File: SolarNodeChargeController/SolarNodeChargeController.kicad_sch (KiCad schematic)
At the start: 36 parts, among them J1 Solar_5V, J2 Solar_5V, J3 Solar_5V, J4 Solar_5V, J5 LiPo_1S_4.2V, J6 VOUT, J7 SW_BATT, J8 SW_LOAD, J9 I2C_MCU, Q1 AO3401A, SW3 SOLAR / BATT, U1 CN3791, U2 INA219AID

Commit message: feat: shrink board to 42x26 mm with SMD diodes and 1.25 mm connectors
Input diodes: D5-D8 move from DO-41 1N5819 to SOD-323 1N5819WS (same
40V/1A rating and pinout). The panels peak at ~200-300 mA each, so the
large through-hole part bought nothing and cost ~12 mm of board width.

Connectors: every power connector (solar J1-J4, battery J5, VOUT J6,
switch leads J7/J8) becomes a 2-pin Micro JST 1.25 / Molex PicoBlade
vertical header (53047-0210), and the I2C header J9 a 4-pin one
(53047-0410). The trade-off is that power connectors are no longer
keyed against each other, so the docs call for clear silkscreen labels.

Charge current: R5 0.12R -> 0.15R lowers it from 1.0 A to 0.8 A, leaving
margin on the 1.0 A-rated PicoBlade contacts on the battery path.

The placement draft is rebuilt around the smaller parts: 60x29 -> 42x26
mm, 0 courtyard overlaps, 0 schematic-parity issues, ERC clean.

gen-schematic.js now derives UUIDs from each item's identity (symbol
ref, wire endpoints, label name and position) instead of random ones.
Regenerating an unchanged design is byte-identical, and symbol UUIDs,
which the PCB footprints link to, no longer churn on every run.

README, CLAUDE.md and the README images are updated to match. The
.kicad_pro change is KiCad writing its default settings when the
project was opened.

Co-Authored-By: Claude Opus 5.5 <noreply@anthropic.com>
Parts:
- removed D5, D6, D7, D8: 1N5819, Diode_THT:D_DO-41_SOD81_P10.16mm_Horizontal, symbol Diode:1N5819
- added D5, D6, D7, D8: 1N5819WS, Diode_SMD:D_SOD-323, symbol Diode:1N5819WS
- J1, J2, J3, J4, J5, J6: footprint Connector_JST:JST_PH_B2B-PH-K_1x02_P2.00mm_Vertical -> Connector_Molex:Molex_PicoBlade_53047-0210_1x02_P1.25mm_Vertical
- J7, J8: footprint Connector_JST:JST_XH_B2B-XH-A_1x02_P2.50mm_Vertical -> Connector_Molex:Molex_PicoBlade_53047-0210_1x02_P1.25mm_Vertical
- J9: footprint Connector_PinHeader_2.54mm:PinHeader_1x04_P2.54mm_Vertical -> Connector_Molex:Molex_PicoBlade_53047-0410_1x04_P1.25mm_Vertical
- R5: value 0.12R 1% -> 0.15R 1%
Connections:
- net PV: now also D5.1 (K), D6.1 (K), D7.1 (K), D8.1 (K)
- net at J3.1 (Pin_1): now also D7.2 (A)
- net at J1.1 (Pin_1): now also D5.2 (A)
- net at J4.1 (Pin_1): now also D8.2 (A)
- net at J2.1 (Pin_1): now also D6.2 (A)
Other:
- note added: "Design notes (CN3791 datasheet, Figure 1): - Solar inputs J1-J4: up to four 5V panels in parallel, each isolated by a 1N5819WS (SOD-323, 40V/1A). MPPT senses VIN after these diodes, so each panel sits ~0.3-0.45V above the 4.6V setpoint (~4.9-5.0V, typical Vmp of a 5V panel). Panels peak at ~200-300mA each. - Charge current: ICH = 120mV / R5 = 120mV / 0.15R = 0.8A, leaving margin on the 1.0A conne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"
- note removed: "Design notes (CN3791 datasheet, Figure 1): - Solar inputs J1-J4: up to four 5V panels in parallel, each isolated by a 1N5819 (40V/1A). MPPT senses VIN after these diodes, so each panel sits ~0.3-0.45V above the 4.6V setpoint (~4.9-5.0V, typical Vmp of a 5V panel). One panel alone carries ~0.9A at 1A charge. - Charge current: ICH = 120mV / R5 = 120mV / 0.12R = 1.0A (R5 = 0.24R for 0.5A). - MPPT se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"
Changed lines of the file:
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@@
 		)
 	)
-	(text "Design notes (CN3791 datasheet, Figure 1):\n- Solar inputs J1-J4: up to four 5V panels in parallel, each isolated by a 1N5819 (40V/1A). MPPT senses VIN after these diodes,\n  so each panel sits ~0.3-0.45V above the 4.6V setpoint (~4.9-5.0V, typical Vmp of a 5V panel). One panel alone carries ~0.9A at 1A charge.\n- Charge current: ICH = 120mV / R5 = 120mV / 0.12R = 1.0A (R5 = 0.24R for 0.5A).\n- MPPT setpoint: VMPPT = 1.205V x (1 + R3/R4) = 1.205 x (1 + 28.0k/10k) = 4.58V. Charging starts once MPPT > 1.23V (VIN > 4.68V).\n- L1: datasheet requires L > 5 x (VCC - VBAT) uH = 16uH at 6V Voc / 2.8V batt. 22uH gives ~0.2A ripple at 6V in, 3.7V batt.\n- Datasheet blocking diode D1 omitted to save ~0.4V headroom: D5-D8 keep the battery out of the panels; the CN3791 then draws ~21uA\n  from the battery via L1 and Q1's body diode when dark (datasheet p.9). Reference D1 is intentionally unused.\n- Status: D4 red ON = charging, D3 green ON = charge done. Both off = no input or VIN < VBAT.\n- Panel-mount SPST switches plug into J7/J8 (JST-XH, 3A; PH is used for panels/battery so leads can't be swapped).\n  J7 SW_BATT isolates the cell from charger and load. J8 SW_LOAD switches only VOUT (J6), so the cell keeps charging with it off.\n  Rate both switches >= 1A or the module's peak current, whichever is higher (battery current is charge OR load, not the sum).\n  With SW_BATT off in sun the CN3791 sees no battery and VBAT pulses near 4.2V: keep SW_LOAD off then.\n- INA219 (U2, I2C 0x40 with A0=A1=GND). SW3 selects the shunt: SOLAR = R7 (PV -> VIN), current from the panels, bus voltage = VIN;\n  BATT = R6 (BATT+ -> cell), + charging / - discharging, bus voltage = cell voltage (readable even with SW_BATT open).\n  Shunts 0.1R match the common INA219 breakout, so stock library calibration (32V/2A, PGA /8 = +/-320mV = +/-3.2A) works as-is.\n  J9 to MCU: 1 VCC_MCU (3.3-5V, powers U2 and pull-ups), 2 SDA, 3 SCL, 4 GND. R8/R9 10k pull-ups: omit if the MCU board has them."
+	(text "Design notes (CN3791 datasheet, Figure 1):\n- Solar inputs J1-J4: up to four 5V panels in parallel, each isolated by a 1N5819WS (SOD-323, 40V/1A). MPPT senses VIN after these diodes,\n  so each panel sits ~0.3-0.45V above the 4.6V setpoint (~4.9-5.0V, typical Vmp of a 5V panel). Panels peak at ~200-300mA each.\n- Charge current: ICH = 120mV / R5 = 120mV / 0.15R = 0.8A, leaving margin on the 1.0A connector contacts (R5 = 0.24R for 0.5A).\n- MPPT setpoint: VMPPT = 1.205V x (1 + R3/R4) = 1.205 x (1 + 28.0k/10k) = 4.58V. Charging starts once MPPT > 1.23V (VIN > 4.68V).\n- L1: datasheet requires L > 5 x (VCC - VBAT) uH = 16uH at 6V Voc / 2.8V batt. 22uH gives ~0.2A ripple at 6V in, 3.7V batt.\n- Datasheet blocking diode D1 omitted to save ~0.4V headroom: D5-D8 keep the battery out of the panels; the CN3791 then draws ~21uA\n  from the battery via L1 and Q1's body diode when dark (datasheet p.9). Reference D1 is intentionally unused.\n- Status: D4 red ON = charging, D3 green ON = charge done. Both off = no input or VIN < VBAT.\n- All power connectors (J1-J8) are 2-pin Micro JST 1.25 / PicoBlade-compatible (1.0A per contact); J9 I2C is the 4-pin version.\n  Panel-mount SPST switches plug into J7/J8. Same connector family everywhere, so check the silkscreen before plugging in.\n  J7 SW_BATT isolates the cell from charger and load. J8 SW_LOAD switches only VOUT (J6), so the cell keeps charging with it off.\n  Rate both switches >= 1A or the module's peak current, whichever is higher (battery current is charge OR load, not the sum).\n  With SW_BATT off in sun the CN3791 sees no battery and VBAT pulses near 4.2V: keep SW_LOAD off then.\n- INA219 (U2, I2C 0x40 with A0=A1=GND). SW3 selects the shunt: SOLAR = R7 (PV -> VIN), current from the panels, bus voltage = VIN;\n  BATT = R6 (BATT+ -> cell), + charging / - discharging, bus voltage = cell voltage (readable even with SW_BATT open).\n  Shunts 0.1R match the common INA219 breakout, so stock library calibration (32V/2A, PGA /8 = +/-320mV = +/-3.2A) works as-is.\n  J9 to MCU: 1 VCC_MCU (3.3-5V, powers U2 and pull-ups), 2 SDA, 3 SCL, 4 GND. R8/R9 10k pull-ups: omit if the MCU board has them."
 		(exclude_from_sim no)
 		(at 40.64 157.48 0)
@@
 			)
 		)
-		(property "Footprint" "Connector_JST:JST_PH_B2B-PH-K_1x02_P2.00mm_Vertical"
+		(property "Footprint" "Connector_Molex:Molex_PicoBlade_53047-0210_1x02_P1.25mm_Vertical"
 			(at 25.4 60.96 0)
 			(hide yes)
@@
 	)
 	(symbol
-		(lib_id "Diode:1N5819")
+		(lib_id "Diode:1N5819WS")
 		(at 39.37 60.96 180)
 		(unit 1)
@@
 			)
 		)
-		(property "Value" "1N5819"
+		(property "Value" "1N5819WS"
 			(at 39.37 64.77 0)
 			(effects
@@
 			)
 		)
-		(property "Footprint" "Diode_THT:D_DO-41_SOD81_P10.16mm_Horizontal"
+		(property "Footprint" "Diode_SMD:D_SOD-323"
 			(at 39.37 60.96 0)
 			(hide yes)
@@
 			)
 		)
-		(property "Datasheet" "http://www.vishay.com/docs/88525/1n5817.pdf"
+		(property "Datasheet" "https://datasheet.lcsc.com/lcsc/2204281430_Guangdong-Hottech-1N5819WS_C191023.pdf"
 			(at 39.37 60.96 0)
 			(hide yes)
@@
 			)
 		)
-		(property "Description" "40V 1A Schottky Barrier Rectifier Diode, DO-41"
+		(property "Description" "40V 600mV@1A 1A SOD-323 Schottky Barrier Diodes, SOD-323"
 			(at 39.37 60.96 0)
 			(hide yes)
@@
 			)
 		)
-		(property "Footprint" "Connector_JST:JST_PH_B2B-PH-K_1x02_P2.00mm_Vertical"
+		(property "Footprint" "Connector_Molex:Molex_PicoBlade_53047-0210_1x02_P1.25mm_Vertical"
 			(at 25.4 73.66 0)
 			(hide yes)
@@
 	)
 	(symbol
-		(lib_id "Diode:1N5819")
+		(lib_id "Diode:1N5819WS")
 		(at 39.37 73.66 180)
 		(unit 1)
@@
 			)
 		)
-		(property "Value" "1N5819"
+		(property "Value" "1N5819WS"
 			(at 39.37 77.47 0)
 			(effects
@@
 			)
 		)
-		(property "Footprint" "Diode_THT:D_DO-41_SOD81_P10.16mm_Horizontal"
+		(property "Footprint" "Diode_SMD:D_SOD-323"
 			(at 39.37 73.66 0)
 			(hide yes)
@@
 			)
 		)
-		(property "Datasheet" "http://www.vishay.com/docs/88525/1n5817.pdf"
+		(property "Datasheet" "https://datasheet.lcsc.com/lcsc/2204281430_Guangdong-Hottech-1N5819WS_C191023.pdf"
 			(at 39.37 73.66 0)
 			(hide yes)
@@
 			)
 		)
-		(property "Description" "40V 1A Schottky Barrier Rectifier Diode, DO-41"
+		(property "Description" "40V 600mV@1A 1A SOD-323 Schottky Barrier Diodes, SOD-323"
 			(at 39.37 73.66 0)
 			(hide yes)
@@
 			)
 		)
-		(property "Footprint" "Connector_JST:JST_PH_B2B-PH-K_1x02_P2.00mm_Vertical"
+		(property "Footprint" "Connector_Molex:Molex_PicoBlade_53047-0210_1x02_P1.25mm_Vertical"
 			(at 25.4 86.36 0)
 			(hide yes)
@@
 	)
 	(symbol
-		(lib_id "Diode:1N5819")
+		(lib_id "Diode:1N5819WS")
 		(at 39.37 86.36 180)
 		(unit 1)
@@
 			)
 		)
-		(property "Value" "1N5819"
+		(property "Value" "1N5819WS"
 			(at 39.37 90.17 0)
 			(effects
@@
 			)
 		)
-		(property "Footprint" "Diode_THT:D_DO-41_SOD81_P10.16mm_Horizontal"
+		(property "Footprint" "Diode_SMD:D_SOD-323"
 			(at 39.37 86.36 0)
 			(hide yes)
@@
 			)
 		)
-		(property "Datasheet" "http://www.vishay.com/docs/88525/1n5817.pdf"
+		(property "Datasheet" "https://datasheet.lcsc.com/lcsc/2204281430_Guangdong-Hottech-1N5819WS_C191023.pdf"
 			(at 39.37 86.36 0)
 			(hide yes)
@@
 			)
 		)
-		(property "Description" "40V 1A Schottky Barrier Rectifier Diode, DO-41"
+		(property "Description" "40V 600mV@1A 1A SOD-323 Schottky Barrier Diodes, SOD-323"
 			(at 39.37 86.36 0)
 			(hide yes)
@@
 			)
 		)
-		(property "Footprint" "Connector_JST:JST_PH_B2B-PH-K_1x02_P2.00mm_Vertical"
+		(property "Footprint" "Connector_Molex:Molex_PicoBlade_53047-0210_1x02_P1.25mm_Vertical"
 			(at 25.4 99.06 0)
 			(hide yes)
@@
 	)
 	(symbol
-		(lib_id "Diode:1N5819")
+		(lib_id "Diode:1N5819WS")
 		(at 39.37 99.06 180)
 		(unit 1)
@@
 			)
 		)
-		(property "Value" "1N5819"
+		(property "Value" "1N5819WS"
 			(at 39.37 102.87 0)
 			(effects
@@
 			)
 		)
-		(property "Footprint" "Diode_THT:D_DO-41_SOD81_P10.16mm_Horizontal"
+		(property "Footprint" "Diode_SMD:D_SOD-323"
 			(at 39.37 99.06 0)
 			(hide yes)
@@
 			)
 		)
-		(property "Datasheet" "http://www.vishay.com/docs/88525/1n5817.pdf"
+		(property "Datasheet" "https://datasheet.lcsc.com/lcsc/2204281430_Guangdong-Hottech-1N5819WS_C191023.pdf"
 			(at 39.37 99.06 0)
 			(hide yes)
@@
 			)
 		)
-		(property "Description" "40V 1A Schottky Barrier Rectifier Diode, DO-41"
+		(property "Description" "40V 600mV@1A 1A SOD-323 Schottky Barrier Diodes, SOD-323"
 			(at 39.37 99.06 0)
 			(hide yes)
@@
 			)
 		)
-		(property "Value" "0.12R 1%"
+		(property "Value" "0.15R 1%"
 			(at 176.53 54.61 270)
 			(effects
@@
 			)
 		)
-		(property "Footprint" "Connector_JST:JST_XH_B2B-XH-A_1x02_P2.50mm_Vertical"
+		(property "Footprint" "Connector_Molex:Molex_PicoBlade_53047-0210_1x02_P1.25mm_Vertical"
 			(at 226.06 50.8 0)
 			(hide yes)
@@
 			)
 		)
-		(property "Footprint" "Connector_JST:JST_PH_B2B-PH-K_1x02_P2.00mm_Vertical"
+		(property "Footprint" "Connector_Molex:Molex_PicoBlade_53047-0210_1x02_P1.25mm_Vertical"
 			(at 226.06 68.58 0)
 			(hide yes)
@@
 			)
 		)
-		(property "Footprint" "Connector_JST:JST_XH_B2B-XH-A_1x02_P2.50mm_Vertical"
+		(property "Footprint" "Connector_Molex:Molex_PicoBlade_53047-0210_1x02_P1.25mm_Vertical"
 			(at 226.06 86.36 0)
 			(hide yes)
@@
 			)
 		)
-		(property "Footprint" "Connector_JST:JST_PH_B2B-PH-K_1x02_P2.00mm_Vertical"
+		(property "Footprint" "Connector_Molex:Molex_PicoBlade_53047-0210_1x02_P1.25mm_Vertical"
 			(at 251.46 86.36 0)
 			(hide yes)
@@
 			)
 		)
-		(property "Footprint" "Connector_PinHeader_2.54mm:PinHeader_1x04_P2.54mm_Vertical"
+		(property "Footprint" "Connector_Molex:Molex_PicoBlade_53047-0410_1x04_P1.25mm_Vertical"
 			(at 393.7 101.6 0)
 			(hide yes)

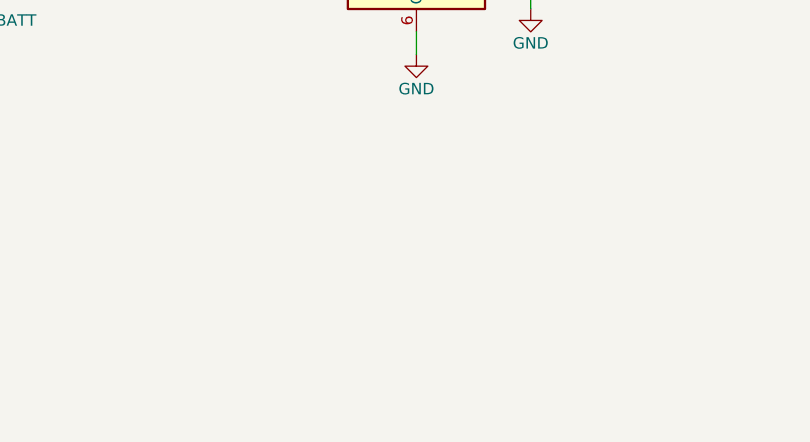
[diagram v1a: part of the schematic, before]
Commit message: feat(pcb): route the board, add M3 holes, silkscreen and fab packaging
Board: grows to 56.5 x 29 mm with 2 mm corner chamfers and four
non-plated M3 holes (H1-H4, added to the schematic as MountingHole
symbols, excluded from the BOM). The holes sit in 7.5 mm end bands that
also take SW3 and the I2C connector J9.

Routing: tools/route-pcb.py is a grid A* router written for this board,
since no FreeRouting/Java is available here. It fans GND out first (an
F.Cu stub and via per SMD GND pad; routing signals first left U2 pin 6
boxed in), routes power nets at 0.8 mm (0.4 mm into small pads) and
signals at 0.25 mm, Kelvin-connects the sense pins to R5/R6/R7, and pours
GND on both layers. A turn penalty keeps runs straight/45 degrees, and
B.Cu/via costs keep 80% of copper on F.Cu so the plane stays mostly
whole. Result: 206 segments, 45 vias; DRC 0 violations, 0 unconnected,
schematic parity 0. Power-connector GND pins connect solidly to the
pours, which also fixes starved thermals on the small PicoBlade pads.

Silkscreen: place-pcb.py now places every reference label itself (first
clear side, fine nudges) instead of leaving library positions that
overlapped neighbours. Function labels SW_BATT/SW_LOAD/BATT/VOUT/I2C, one
Solar_5V label with a bracket over J1-J4, I2C pin names and a
"solar/batt / i2c power sensor" label for SW3 on the back (solar at the
PV throws), and the module ID "Solar Charge Module v1.0 / by
JaisorGadgets / Oct. 2026" on the back.

Fabrication: tools/fab-package.js turns the kicad-cli exports into a
JLCPCB-style BOM/CPL, writes fab notes and zips Gerbers + drill files.
The package itself stays in gitignored output/ for a release tag.

gen-schematic.js copies each symbol's in_bom flag from its library, which
keeps parity clean for the mounting holes. README and CLAUDE.md cover the
full regeneration pipeline, routing, labels and fabrication; images are
re-rendered, including a new bottom view. The .kicad_pro change is KiCad
saving its default settings.

C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
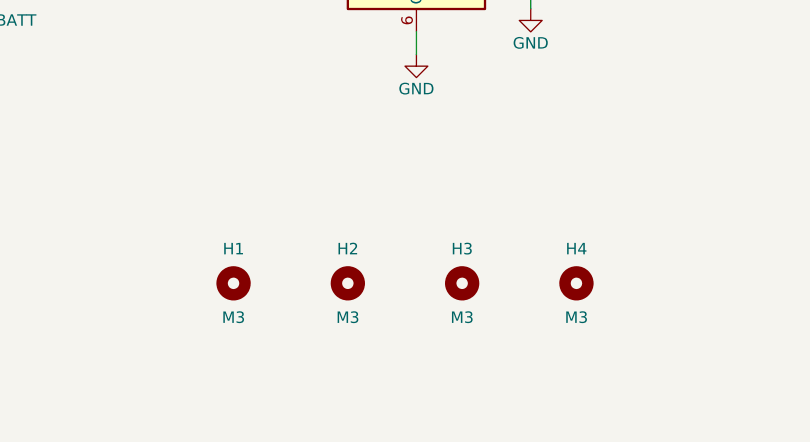
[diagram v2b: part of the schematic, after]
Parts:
- added H1, H2, H3, H4: M3, MountingHole:MountingHole_3.2mm_M3, symbol Mechanical:MountingHole
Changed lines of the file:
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@@
+	)
+	(symbol
+		(lib_id "Mechanical:MountingHole")
+		(at 302.26 142.24 0)
+		(unit 1)
+		(exclude_from_sim no)
+		(in_bom no)
+		(on_board yes)
+		(dnp no)
+		(property "Reference" "H1"
+			(at 302.26 138.43 0)
+			(effects
+				(font
+					(size 1.27 1.27)
+				)
+			)
+		)
+		(property "Value" "M3"
+			(at 302.26 146.05 0)
+			(effects
+				(font
+					(size 1.27 1.27)
+				)
+			)
+		)
+		(property "Footprint" "MountingHole:MountingHole_3.2mm_M3"
+			(at 302.26 142.24 0)
+			(hide yes)
+			(effects
+				(font
+					(size 1.27 1.27)
+				)
+			)
+		)
+		(property "Datasheet" "~"
+			(at 302.26 142.24 0)
+			(hide yes)
+			(effects
+				(font
+					(size 1.27 1.27)
+				)
+			)
+		)
+		(property "Description" "Mounting Hole without connection"
+			(at 302.26 142.24 0)
+			(hide yes)
+			(effects
+				(font
+					(size 1.27 1.27)
+				)
+			)
+		)
+		(instances
+			(project "SolarNodeChargeController"
+				(path "/94501acb-e983-4695-a18c-1a4d3ecd2660"
+					(reference "H1")
+					(unit 1)
+				)
+			)
+		)
+	)
+	(symbol
+		(lib_id "Mechanical:MountingHole")
+		(at 314.96 142.24 0)
+		(unit 1)
+		(exclude_from_sim no)
+		(in_bom no)
+		(on_board yes)
+		(dnp no)
+		(property "Reference" "H2"
+			(at 314.96 138.43 0)
+			(effects
+				(font
+					(size 1.27 1.27)
+				)
+			)
+		)
+		(property "Value" "M3"
+			(at 314.96 146.05 0)
+			(effects
+				(font
+					(size 1.27 1.27)
+				)
+			)
+		)
+		(property "Footprint" "MountingHole:MountingHole_3.2mm_M3"
+			(at 314.96 142.24 0)
+			(hide yes)
+			(effects
+				(font
+					(size 1.27 1.27)
+				)
+			)
+		)
+		(property "Datasheet" "~"
+			(at 314.96 142.24 0)
+			(hide yes)
+			(effects
+				(font
+					(size 1.27 1.27)
+				)
+			)
+		)
+		(property "Description" "Mounting Hole without connection"
+			(at 314.96 142.24 0)
+			(hide yes)
+			(effects
+				(font
+					(size 1.27 1.27)
+				)
+			)
+		)
+		(instances
+			(project "SolarNodeChargeController"
+				(path "/94501acb-e983-4695-a18c-1a4d3ecd2660"
+					(reference "H2")
+					(unit 1)
+				)
+			)
+		)
+	)
+	(symbol
+		(lib_id "Mechanical:MountingHole")
+		(at 327.66 142.24 0)
+		(unit 1)
+		(exclude_from_sim no)
+		(in_bom no)
+		(on_board yes)
+		(dnp no)
+		(property "Reference" "H3"
+			(at 327.66 138.43 0)
+			(effects
+				(font
+					(size 1.27 1.27)
+				)
+			)
+		)
+		(property "Value" "M3"
+			(at 327.66 146.05 0)
+			(effects
+				(font
+					(size 1.27 1.27)
+				)
+			)
+		)
+		(property "Footprint" "MountingHole:MountingHole_3.2mm_M3"
+			(at 327.66 142.24 0)
+			(hide yes)
+			(effects
+				(font
+					(size 1.27 1.27)
+				)
+			)
+		)
+		(property "Datasheet" "~"
+			(at 327.66 142.24 0)
+			(hide yes)
+			(effects
+				(font
+					(size 1.27 1.27)
+				)
+			)
+		)
+		(property "Description" "Mounting Hole without connection"
+			(at 327.66 142.24 0)
+			(hide yes)
+			(effects
+				(font
+					(size 1.27 1.27)
+				)
+			)
+		)
+		(instances
+			(project "SolarNodeChargeController"
+				(path "/94501acb-e983-4695-a18c-1a4d3ecd2660"
+					(reference "H3")
+					(unit 1)
+				)
+			)
+		)
+	)
+	(symbol
+		(lib_id "Mechanical:MountingHole")
+		(at 340.36 142.24 0)
+		(unit 1)
+		(exclude_from_sim no)
+		(in_bom no)
+		(on_board yes)
+		(dnp no)
+		(property "Reference" "H4"
+			(at 340.36 138.43 0)
+			(effects
+				(font
+					(size 1.27 1.27)
+				)
+			)
+		)
+		(property "Value" "M3"
+			(at 340.36 146.05 0)
+			(effects
+				(font
+					(size 1.27 1.27)
+				)
+			)
+		)
+		(property "Footprint" "MountingHole:MountingHole_3.2mm_M3"
+			(at 340.36 142.24 0)
+			(hide yes)
+			(effects
+				(font
+					(size 1.27 1.27)
+				)
+			)
+		)
+		(property "Datasheet" "~"
+			(at 340.36 142.24 0)
+			(hide yes)
+			(effects
+				(font
+					(size 1.27 1.27)
+				)
+			)
+		)
+		(property "Description" "Mounting Hole without connection"
+			(at 340.36 142.24 0)
+			(hide yes)
+			(effects
+				(font
+					(size 1.27 1.27)
+				)
+			)
+		)
+		(instances
+			(project "SolarNodeChargeController"
+				(path "/94501acb-e983-4695-a18c-1a4d3ecd2660"
+					(reference "H4")
+					(unit 1)
+				)
+			)
+		)
 	)
 	(symbol
